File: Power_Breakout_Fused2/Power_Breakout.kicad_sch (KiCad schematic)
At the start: 16 parts

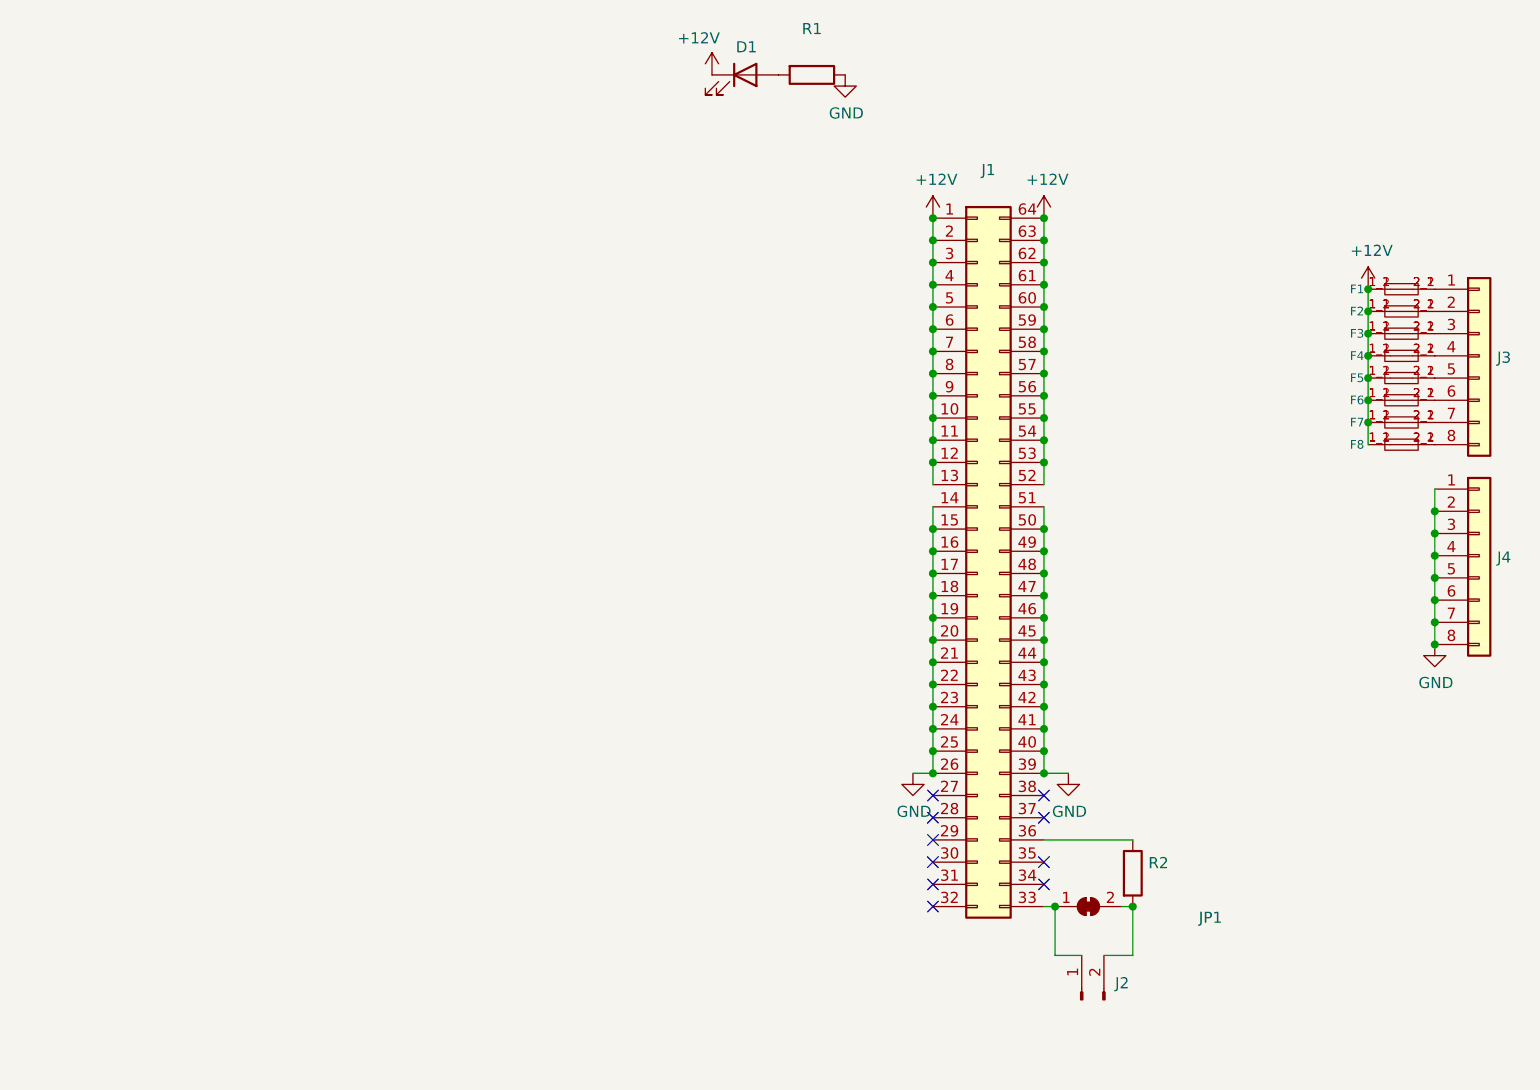
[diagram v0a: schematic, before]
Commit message: added more leds
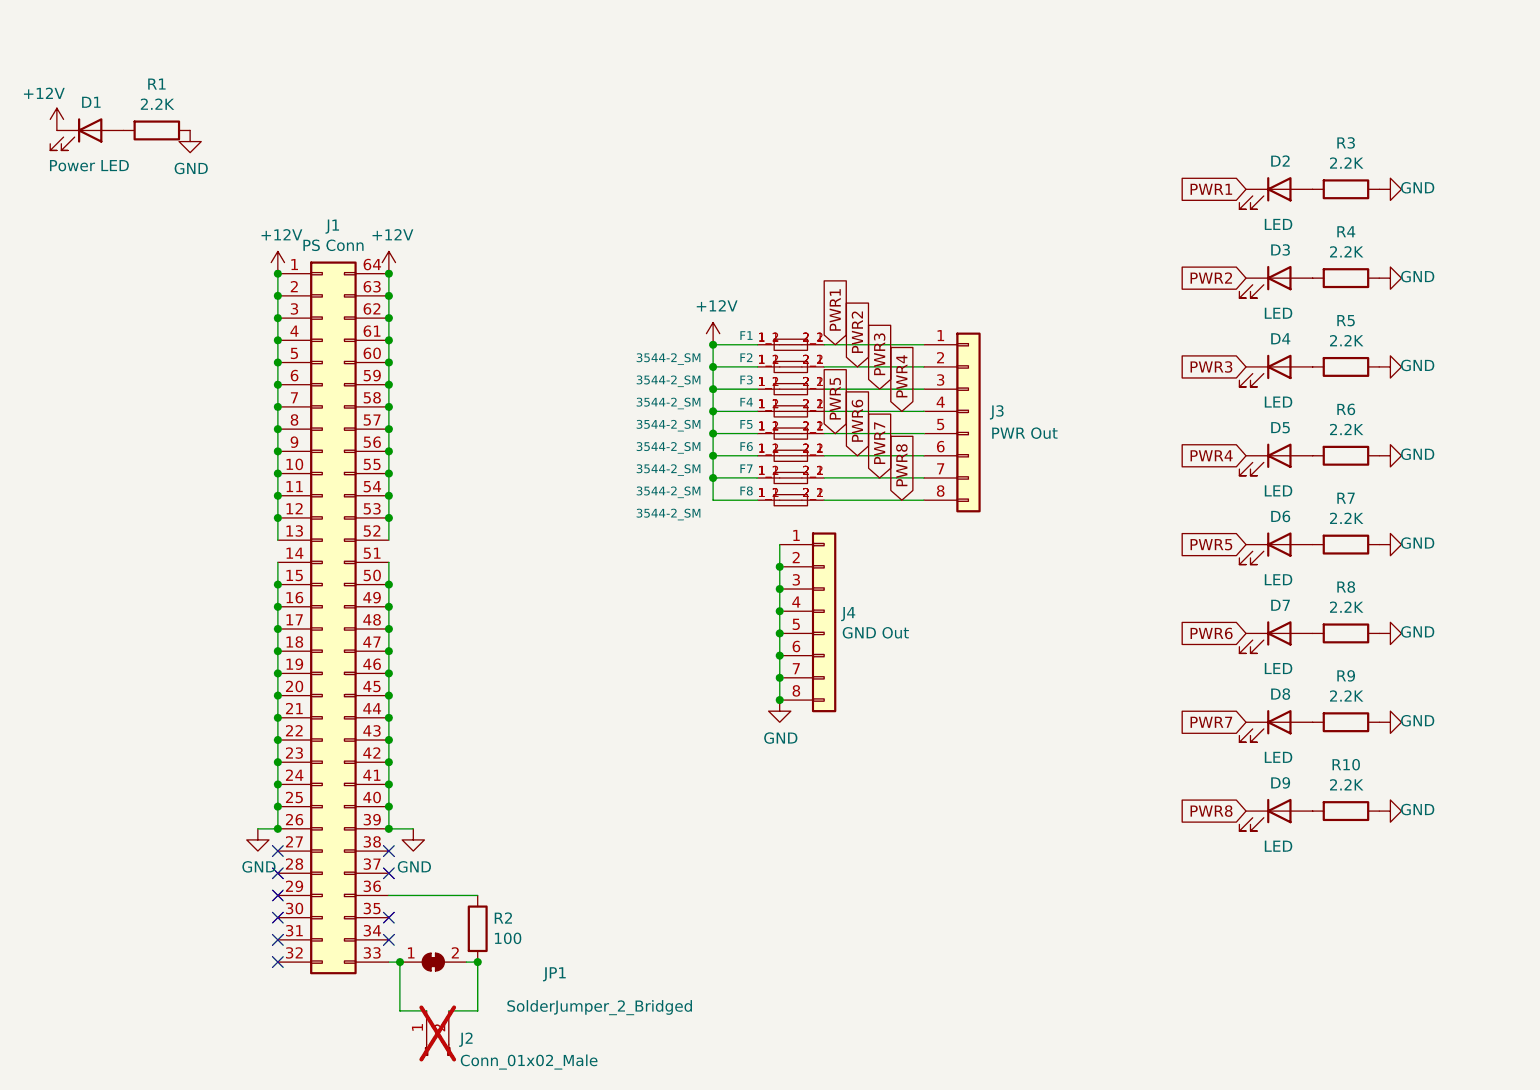
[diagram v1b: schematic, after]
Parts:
- added D2, D3, D4, D5, D6, D7, D8, D9: LED, LED_SMD:LED_0402_1005Metric, symbol Device:LED
- added R10, R3, R4, R5, R6, R7, R8, R9: 2.2K, Resistor_SMD:R_0402_1005Metric, symbol Device:R
- D1: value (none) -> Power LED; footprint (none) -> LED_SMD:LED_0603_1608Metric; Digi-Key PN (none) -> 160-1436-1-ND; LCSC (none) -> C2286; MPN (none) -> LTST-C190KRKT
- F1, F2, F3, F4, F5, F6, F7, F8: value (none) -> 3544-2_SM; footprint (none) -> 3544-2:FUSE_3544-2; LCSC (none) -> C492610; MPN (none) -> 3544-2
- J1: value (none) -> PS Conn; footprint (none) -> TE_1761469-1:TE_1761469-1; Digi-Key PN (none) -> A102052-ND; MPN (none) -> 1761468-1
- J2: value (none) -> Conn_01x02_Male; footprint (none) -> Connector_PinHeader_2.54mm:PinHeader_1x02_P2.54mm_Vertical; now not fitted
- J3: value (none) -> PWR Out; footprint (none) -> Connector_Phoenix_MC_HighVoltage:PhoenixContact_MCV_1,5_8-G-5.08_1x08_P5.08mm_Vertical; MPN (none) -> VI0821550000G
- J4: value (none) -> GND Out; footprint (none) -> Connector_Phoenix_MC_HighVoltage:PhoenixContact_MCV_1,5_8-G-5.08_1x08_P5.08mm_Vertical; MPN (none) -> VI0821550000G
- JP1: value (none) -> SolderJumper_2_Bridged; footprint (none) -> Jumper:SolderJumper-2_P1.3mm_Bridged_Pad1.0x1.5mm
- R1: value (none) -> 2.2K; footprint (none) -> Resistor_SMD:R_0603_1608Metric; Digi-Key PN (none) -> 311-2.20KHRCT-ND; LCSC (none) -> C4190; MPN (none) -> RC0603FR-072K2L
- R2: value (none) -> 100; footprint (none) -> Resistor_SMD:R_0603_1608Metric; Digi-Key PN (none) -> 311-100HRCT-ND; LCSC (none) -> C22775; MPN (none) -> RC0603FR-07100RL
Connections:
- net GND: now also R10.1, R3.1, R4.1, R5.1, R6.1, R7.1, R8.1, R9.1
- net PWR6: now reaches F6.2_1 (2), F6.2_2 (2), J3.6 (Pin_6)
- net PWR6: now also D7.1 (K)
- net PWR1: now reaches F1.2_1 (2), F1.2_2 (2), J3.1 (Pin_1)
- net PWR1: now also D2.1 (K)
- net PWR2: now reaches F2.2_1 (2), F2.2_2 (2), J3.2 (Pin_2)
- net PWR2: now also D3.1 (K)
- net PWR3: now reaches F3.2_1 (2), F3.2_2 (2), J3.3 (Pin_3)
- net PWR3: now also D4.1 (K)
- net PWR4: now reaches F4.2_1 (2), F4.2_2 (2), J3.4 (Pin_4)
- net PWR4: now also D5.1 (K)
- net PWR5: now reaches F5.2_1 (2), F5.2_2 (2), J3.5 (Pin_5)
- net PWR5: now also D6.1 (K)
- net PWR7: now reaches F7.2_1 (2), F7.2_2 (2), J3.7 (Pin_7)
- net PWR7: now also D8.1 (K)
- net PWR8: now reaches F8.2_1 (2), F8.2_2 (2), J3.8 (Pin_8)
- net PWR8: now also D9.1 (K)
- new net: D8.2 (A), R9.2
- new net: D6.2 (A), R7.2
- new net: D5.2 (A), R6.2
- new net: D7.2 (A), R8.2
- new net: D9.2 (A), R10.2
- new net: D4.2 (A), R5.2
- new net: D3.2 (A), R4.2
- new net: D2.2 (A), R3.2
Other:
- company: (none) -> Scott Hanson
- title: (none) -> HP Fused Breakout
- moved on the sheet: D1, F1, F2, F3, F4, F5, F6, F7, F8, J1, J3, J4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
